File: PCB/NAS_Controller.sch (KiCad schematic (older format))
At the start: 0 parts

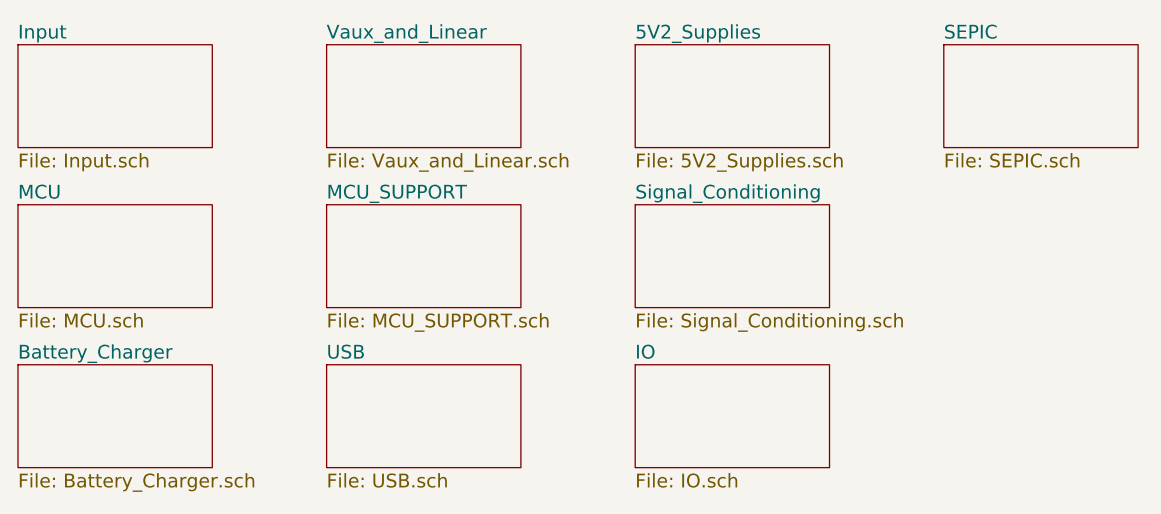
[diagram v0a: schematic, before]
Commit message: Added ELOAD to sch and imported to layout
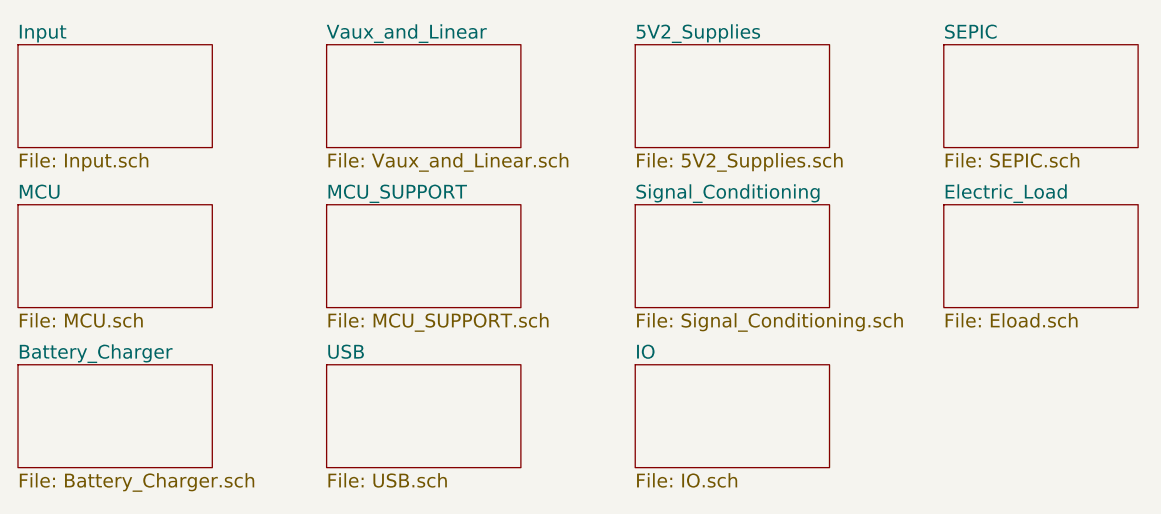
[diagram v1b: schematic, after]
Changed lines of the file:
@@
 $Descr A 11000 8500
 encoding utf-8
-Sheet 1 11
+Sheet 1 12
 Title "NAS Controller"
 Date "2018-06-12"
-Rev "01"
+Rev "02"
 Comp ""
 Comment1 ""
@@
 F1 "SEPIC.sch" 60
 $EndSheet
+$Sheet
+S 7650 3500 850  450
+U 5BF4E0C2
+F0 "Electric_Load" 60
+F1 "Eload.sch" 60
+$EndSheet
 $EndSCHEMATC
